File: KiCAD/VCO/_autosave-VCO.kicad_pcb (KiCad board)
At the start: 2 copper layers, 50 x 100 mm, 42 parts, among them J1 CV IN 1, J2 CV IN 2, J3 PWM, J4 SAW OUT, J5 PULSE OUT, J6 Conn_01x03_Pin, J7 Conn_01x03_Pin, Q1 NPN, T1 PNP, T2 NPN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

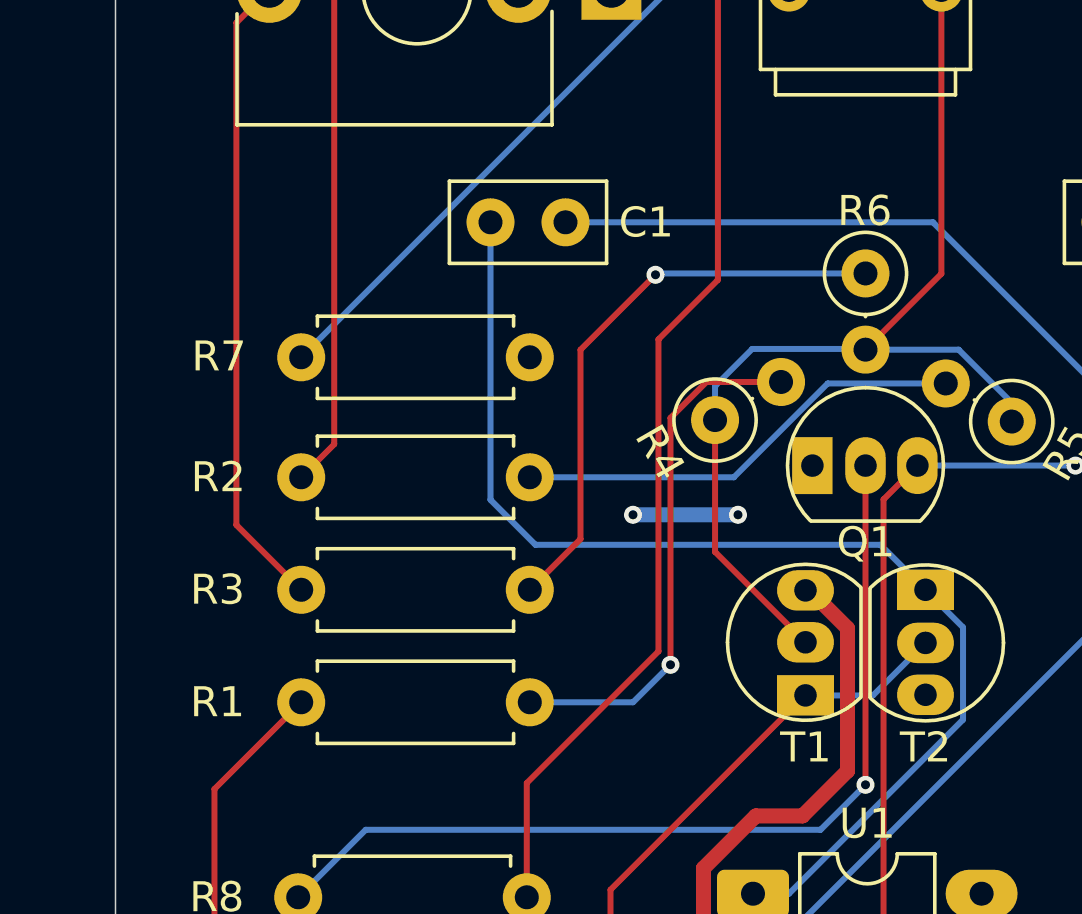
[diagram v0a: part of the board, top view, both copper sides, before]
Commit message: Cleanup resistor references etc
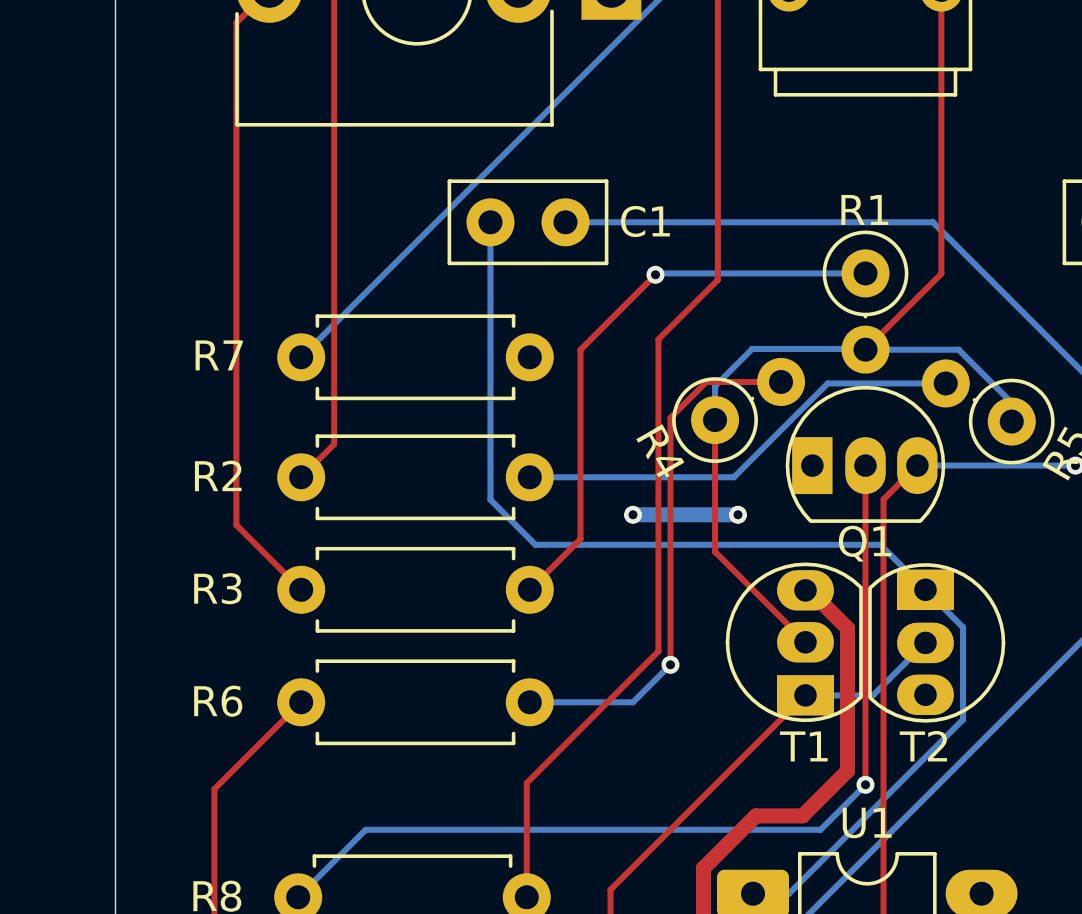
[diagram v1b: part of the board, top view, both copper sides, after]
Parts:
- renumbered R6 to R1, R1 to R6
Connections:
- J6 pad 2: GND -> VDD
- J7 pad 2: GND -> VDD
- Q1 pad 1: GND -> VDD
- R10 pad 1: GND -> VDD
- R13 pad 1: GND -> VDD
- RV3 pad 1: GND -> VDD
- U1 pad 14: GND -> VDD
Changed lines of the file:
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@@
 	(net 18 "Net-(Q1-B)")
 	(net 19 "Net-(Q1-E)")
-	(net 20 "Net-(R1-Pad2)")
+	(net 20 "Net-(R4-Pad2)")
 	(net 21 "Net-(R1-Pad1)")
 	(net 22 "Net-(R2-Pad2)")
-	(net 23 "Net-(R3-Pad2)")
+	(net 23 "Net-(R6-Pad1)")
 	(net 24 "Net-(T1-B)")
 	(net 25 "Net-(R7-Pad1)")
@@
 			(layers "*.Cu" "*.Mask")
 			(remove_unused_layers no)
-			(net 9 "GND")
+			(net 17 "VDD")
 			(pinfunction "1")
 			(pintype "passive")
@@
 			(layers "*.Cu" "*.Mask")
 			(remove_unused_layers no)
-			(net 9 "GND")
+			(net 17 "VDD")
 			(pinfunction "C")
 			(pintype "open_collector")
@@
 			(layers "*.Cu" "*.Mask")
 			(remove_unused_layers no)
-			(net 23 "Net-(R3-Pad2)")
+			(net 21 "Net-(R1-Pad1)")
 			(pintype "passive")
 		)
@@
 			(layers "*.Cu" "*.Mask")
 			(remove_unused_layers no)
-			(net 9 "GND")
+			(net 17 "VDD")
 			(pinfunction "Pin_2")
 			(pintype "passive")
@@
 			(layers "*.Cu" "*.Mask")
 			(remove_unused_layers no)
-			(net 9 "GND")
+			(net 17 "VDD")
 			(pinfunction "VDD")
 			(pintype "power_in")
@@
 			(layers "*.Cu" "*.Mask")
 			(remove_unused_layers no)
-			(net 21 "Net-(R1-Pad1)")
+			(net 23 "Net-(R6-Pad1)")
 			(pinfunction "2")
 			(pintype "passive")
@@
 			(layers "*.Cu" "*.Mask")
 			(remove_unused_layers no)
-			(net 9 "GND")
+			(net 17 "VDD")
 			(pintype "passive")
 		)
@@
 			(layers "*.Cu" "*.Mask")
 			(remove_unused_layers no)
-			(net 20 "Net-(R1-Pad2)")
+			(net 20 "Net-(R4-Pad2)")
 			(pintype "passive")
 		)
@@
 		(descr "Resistor, Axial_DIN0207 series, Axial, Horizontal, pin pitch=7.62mm, 0.25W = 1/4W, length*diameter=6.3*2.5mm^2, http://cdn-reichelt.de/documents/datenblatt/B400/1_4W%23YAG.pdf")
 		(tags "Resistor Axial_DIN0207 series Axial Horizontal pin pitch 7.62mm 0.25W = 1/4W length 6.3mm diameter 2.5mm")
-		(property "Reference" "R1"
+		(property "Reference" "R6"
 			(at -2.79 0 0)
 			(layer "F.SilkS")
@@
 			(layers "*.Cu" "*.Mask")
 			(remove_unused_layers no)
-			(net 21 "Net-(R1-Pad1)")
+			(net 23 "Net-(R6-Pad1)")
 			(pintype "passive")
 		)
@@
 			(layers "*.Cu" "*.Mask")
 			(remove_unused_layers no)
-			(net 20 "Net-(R1-Pad2)")
+			(net 20 "Net-(R4-Pad2)")
 			(pintype "passive")
 		)
@@
 			(layers "*.Cu" "*.Mask")
 			(remove_unused_layers no)
-			(net 9 "GND")
+			(net 17 "VDD")
 			(pintype "passive")
 		)
@@
 		(descr "Resistor, Axial_DIN0207 series, Axial, Vertical, pin pitch=2.54mm, 0.25W = 1/4W, length*diameter=6.3*2.5mm^2, http://cdn-reichelt.de/documents/datenblatt/B400/1_4W%23YAG.pdf")
 		(tags "Resistor Axial_DIN0207 series Axial Vertical pin pitch 2.54mm 0.25W = 1/4W length 6.3mm diameter 2.5mm")
-		(property "Reference" "R6"
+		(property "Reference" "R1"
 			(at -2.08 0.025 180)
 			(layer "F.SilkS")
@@
 			(layers "*.Cu" "*.Mask")
 			(remove_unused_layers no)
-			(net 23 "Net-(R3-Pad2)")
+			(net 21 "Net-(R1-Pad1)")
 			(pintype "passive")
 		)
@@
 			(layers "*.Cu" "*.Mask")
 			(remove_unused_layers no)
-			(net 9 "GND")
+			(net 17 "VDD")
 			(pinfunction "Pin_2")
 			(pintype "passive")
@@
 	)
 	(segment
-		(start 56.19 101.25)
-		(end 53.299 104.141)
+		(start 65.5 89.5)
+		(end 65.5 95.81)
 		(width 0.2)
 		(layer "F.Cu")
@@
 	)
 	(segment
-		(start 58.499 142.999)
-		(end 60 144.5)
+		(start 68 87)
+		(end 65.5 89.5)
 		(width 0.2)
 		(layer "F.Cu")
@@
 	)
 	(segment
-		(start 53.299 104.141)
-		(end 53.299 138.453106)
+		(start 65.5 95.81)
+		(end 63.81 97.5)
 		(width 0.2)
 		(layer "F.Cu")
 		(net 21)
 	)
+	(via
+		(at 68 87)
+		(size 0.6)
+		(drill 0.3)
+		(layers "F.Cu" "B.Cu")
+		(net 21)
+	)
 	(segment
-		(start 57.844894 142.999)
-		(end 58.499 142.999)
+		(start 68.045 86.955)
+		(end 68 87)
 		(width 0.2)
-		(layer "F.Cu")
+		(layer "B.Cu")
 		(net 21)
 	)
 	(segment
-		(start 53.299 138.453106)
-		(end 57.844894 142.999)
+		(start 75 86.955)
+		(end 68.045 86.955)
 		(width 0.2)
-		(layer "F.Cu")
+		(layer "B.Cu")
 		(net 21)
 	)
@@
 	)
 	(segment
-		(start 65.5 89.5)
-		(end 65.5 95.81)
+		(start 56.19 101.25)
+		(end 53.299 104.141)
 		(width 0.2)
 		(layer "F.Cu")
@@
 	)
 	(segment
-		(start 68 87)
-		(end 65.5 89.5)
+		(start 58.499 142.999)
+		(end 60 144.5)
 		(width 0.2)
 		(layer "F.Cu")
@@
 	)
 	(segment
-		(start 65.5 95.81)
-		(end 63.81 97.5)
+		(start 53.299 104.141)
+		(end 53.299 138.453106)
 		(width 0.2)
 		(layer "F.Cu")
 		(net 23)
 	)
-	(via
-		(at 68 87)
-		(size 0.6)
-		(drill 0.3)
-		(layers "F.Cu" "B.Cu")
-		(net 23)
-	)
 	(segment
-		(start 68.045 86.955)
-		(end 68 87)
+		(start 57.844894 142.999)
+		(end 58.499 142.999)
 		(width 0.2)
-		(layer "B.Cu")
+		(layer "F.Cu")
 		(net 23)
 	)
 	(segment
-		(start 75 86.955)
-		(end 68.045 86.955)
+		(start 53.299 138.453106)
+		(end 57.844894 142.999)
 		(width 0.2)
-		(layer "B.Cu")
+		(layer "F.Cu")
 		(net 23)
 	)
